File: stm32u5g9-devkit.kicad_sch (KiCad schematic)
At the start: 0 parts

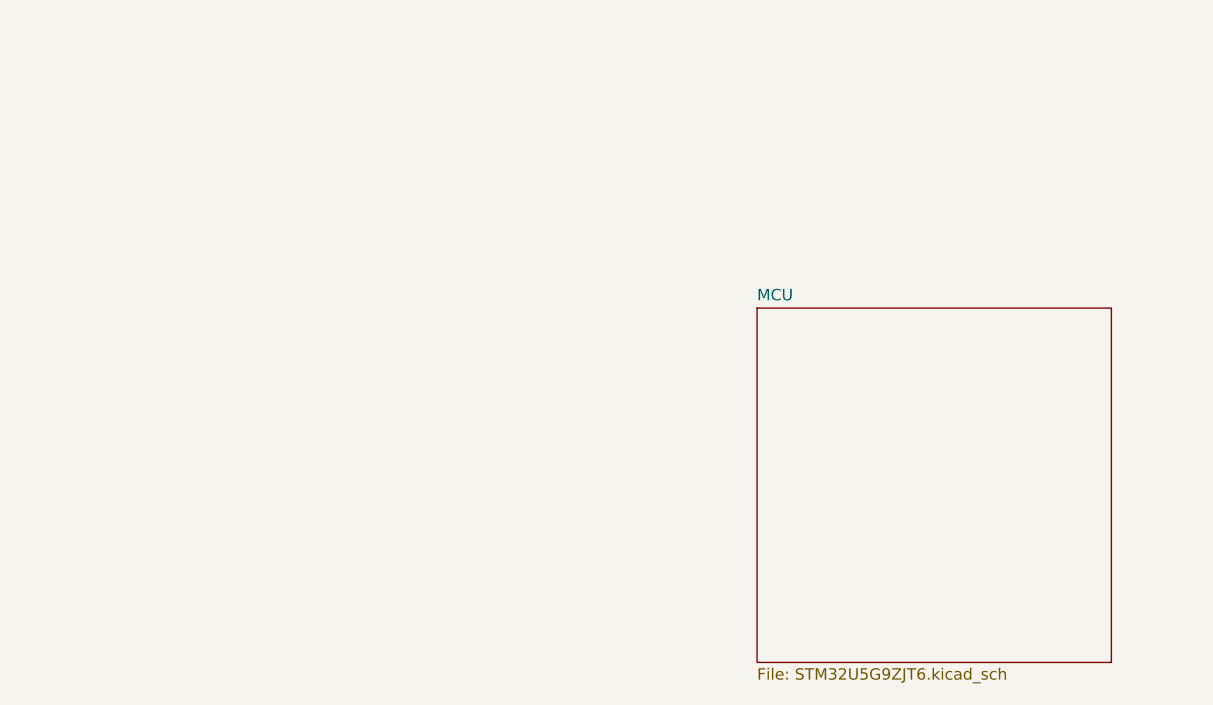
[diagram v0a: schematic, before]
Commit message: Add Octospi Flash, LCD 40P, 50P, MIPI
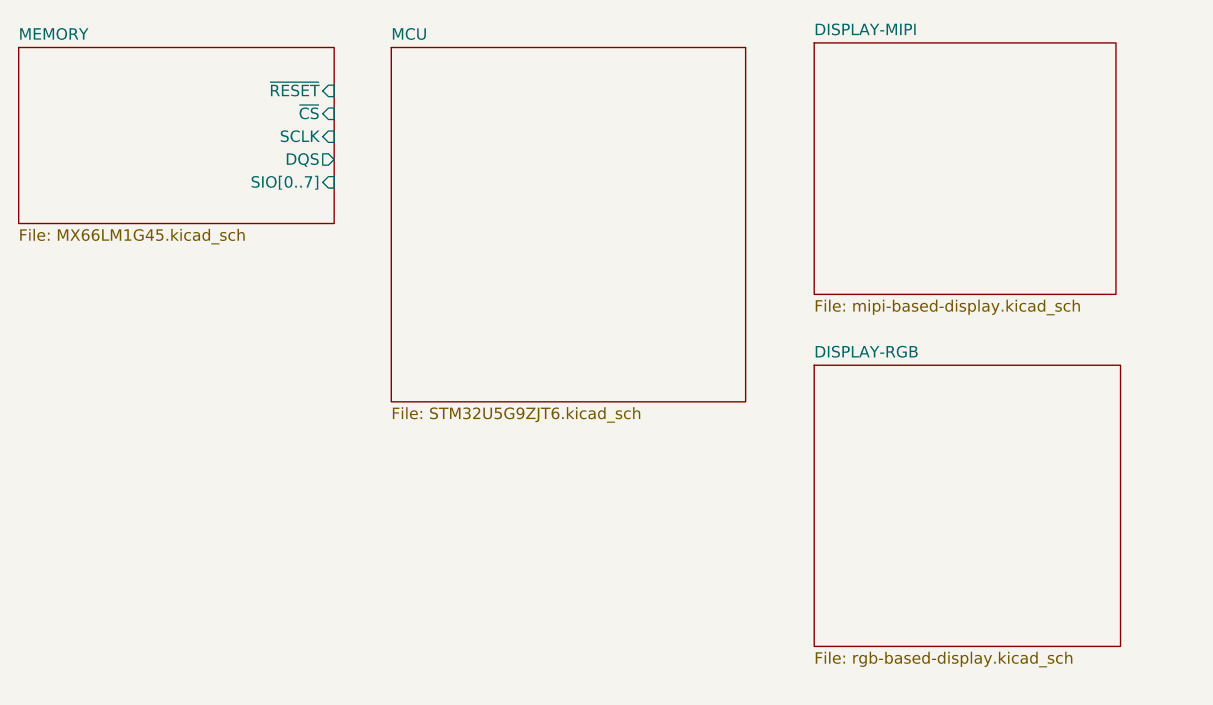
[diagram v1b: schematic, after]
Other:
- added sheet DISPLAY-MIPI (mipi-based-display.kicad_sch)
- added sheet DISPLAY-RGB (rgb-based-display.kicad_sch)
- added sheet MEMORY (MX66LM1G45.kicad_sch)
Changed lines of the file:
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@@
 	(paper "A4")
 	(sheet
-		(at 158.75 92.71)
+		(at 76.708 63.754)
+		(size 35.052 19.558)
+		(fields_autoplaced yes)
+		(stroke
+			(width 0.1524)
+			(type solid)
+		)
+		(fill
+			(color 0 0 0 0.0000)
+		)
+		(property "Sheetname" "MEMORY"
+			(at 76.708 63.0424 0)
+			(effects
+				(font
+					(size 1.27 1.27)
+				)
+				(justify left bottom)
+			)
+		)
+		(property "Sheetfile" "MX66LM1G45.kicad_sch"
+			(at 76.708 83.8966 0)
+			(effects
+				(font
+					(size 1.27 1.27)
+				)
+				(justify left top)
+			)
+		)
+		(pin "SIO[0..7]" input
+			(at 111.76 78.74 0)
+			(effects
+				(font
+					(size 1.27 1.27)
+				)
+				(justify right)
+			)
+		)
+		(pin "SCLK" input
+			(at 111.76 73.66 0)
+			(effects
+				(font
+					(size 1.27 1.27)
+				)
+				(justify right)
+			)
+		)
+		(pin "DQS" output
+			(at 111.76 76.2 0)
+			(effects
+				(font
+					(size 1.27 1.27)
+				)
+				(justify right)
+			)
+		)
+		(pin "~{CS}" input
+			(at 111.76 71.12 0)
+			(effects
+				(font
+					(size 1.27 1.27)
+				)
+				(justify right)
+			)
+		)
+		(pin "~{RESET}" input
+			(at 111.76 68.58 0)
+			(effects
+				(font
+					(size 1.27 1.27)
+				)
+				(justify right)
+			)
+		)
+		(instances
+			(project "stm32u5g9-devkit"
+				(path "/51b81e84-43c5-41b1-a9e5-678506f2d81f"
+					(page "3")
+				)
+			)
+		)
+	)
+	(sheet
+		(at 165.1 63.246)
+		(size 33.528 27.94)
+		(fields_autoplaced yes)
+		(stroke
+			(width 0.1524)
+			(type solid)
+		)
+		(fill
+			(color 0 0 0 0.0000)
+		)
+		(property "Sheetname" "DISPLAY-MIPI"
+			(at 165.1 62.5344 0)
+			(effects
+				(font
+					(size 1.27 1.27)
+				)
+				(justify left bottom)
+			)
+		)
+		(property "Sheetfile" "mipi-based-display.kicad_sch"
+			(at 165.1 91.7706 0)
+			(effects
+				(font
+					(size 1.27 1.27)
+				)
+				(justify left top)
+			)
+		)
+		(instances
+			(project "stm32u5g9-devkit"
+				(path "/51b81e84-43c5-41b1-a9e5-678506f2d81f"
+					(page "4")
+				)
+			)
+		)
+	)
+	(sheet
+		(at 165.1 99.06)
+		(size 34.036 31.242)
+		(fields_autoplaced yes)
+		(stroke
+			(width 0.1524)
+			(type solid)
+		)
+		(fill
+			(color 0 0 0 0.0000)
+		)
+		(property "Sheetname" "DISPLAY-RGB"
+			(at 165.1 98.3484 0)
+			(effects
+				(font
+					(size 1.27 1.27)
+				)
+				(justify left bottom)
+			)
+		)
+		(property "Sheetfile" "rgb-based-display.kicad_sch"
+			(at 165.1 130.8866 0)
+			(effects
+				(font
+					(size 1.27 1.27)
+				)
+				(justify left top)
+			)
+		)
+		(instances
+			(project "stm32u5g9-devkit"
+				(path "/51b81e84-43c5-41b1-a9e5-678506f2d81f"
+					(page "5")
+				)
+			)
+		)
+	)
+	(sheet
+		(at 118.11 63.754)
 		(size 39.37 39.37)
 		(fields_autoplaced yes)
@@
 		)
 		(property "Sheetname" "MCU"
-			(at 158.75 91.9984 0)
+			(at 118.11 63.0424 0)
 			(effects
 				(font
@@
 		)
 		(property "Sheetfile" "STM32U5G9ZJT6.kicad_sch"
-			(at 158.75 132.6646 0)
+			(at 118.11 103.7086 0)
 			(effects
 				(font
